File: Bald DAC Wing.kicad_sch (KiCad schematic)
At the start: 50 parts, among them J1 Power_In, J2 DAC_A_Out, J3 DAC_B_Out, U1 AD5447, U2 AD8065ARTZ, U3 AD8065ARTZ, U4 74LVC574APWR, U5 74LVC574APWR, U6 74LVC14, U7 REF3425

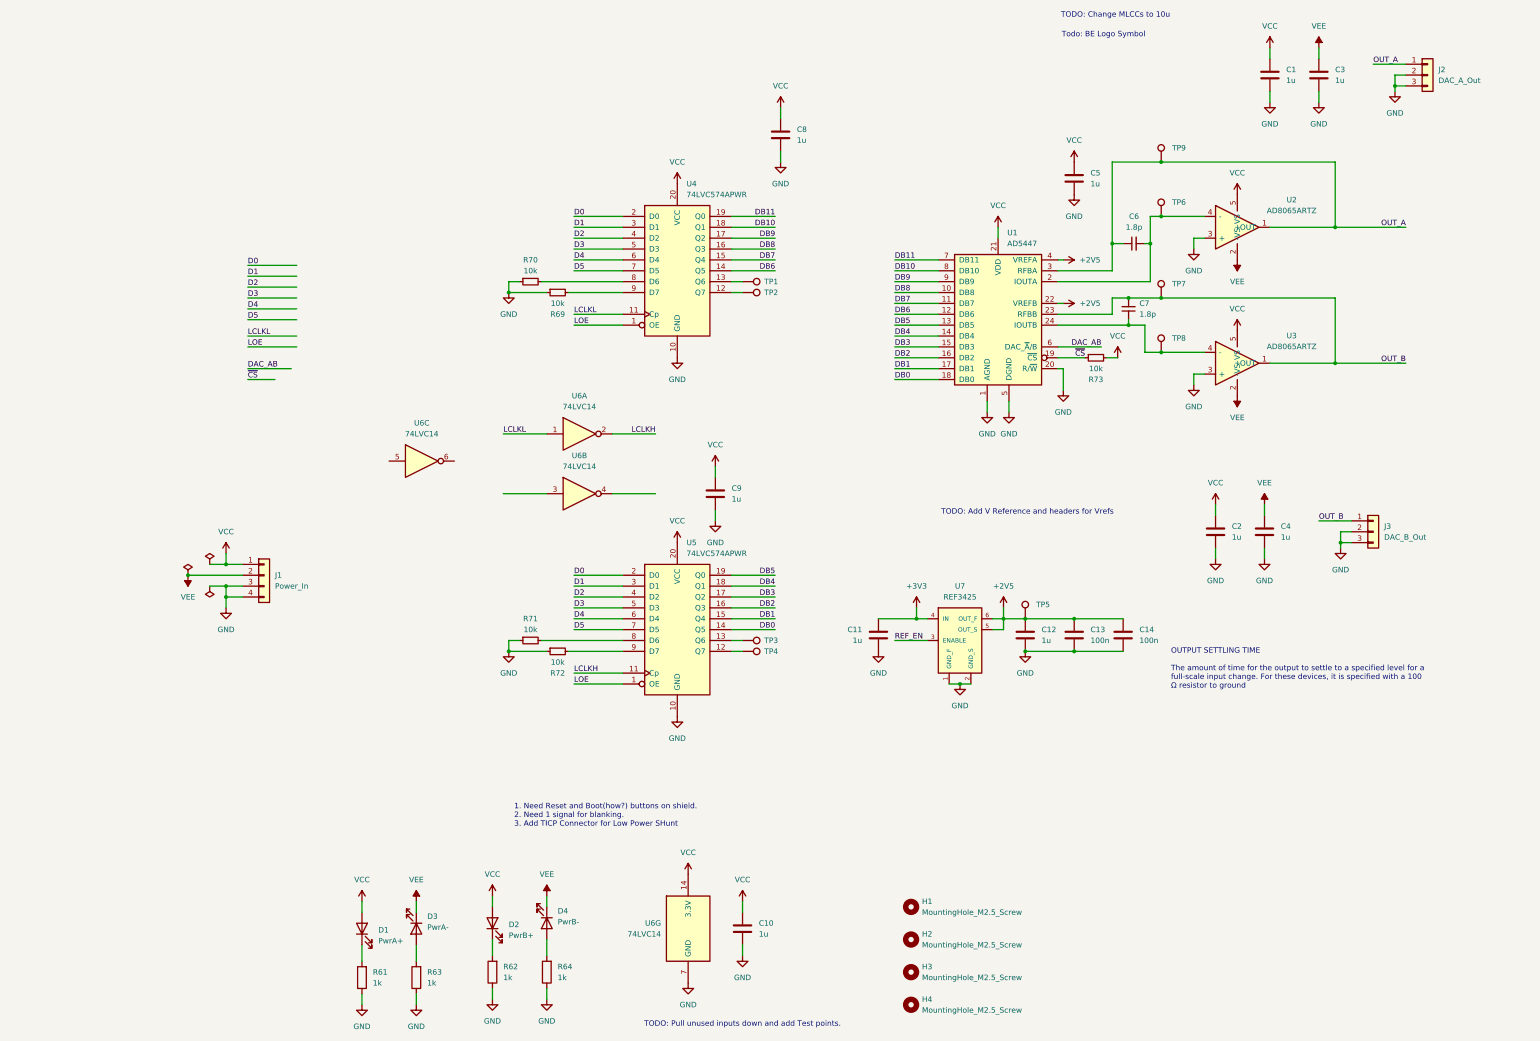
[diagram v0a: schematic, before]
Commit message: updated part numbs and changed to 1 gate inverter
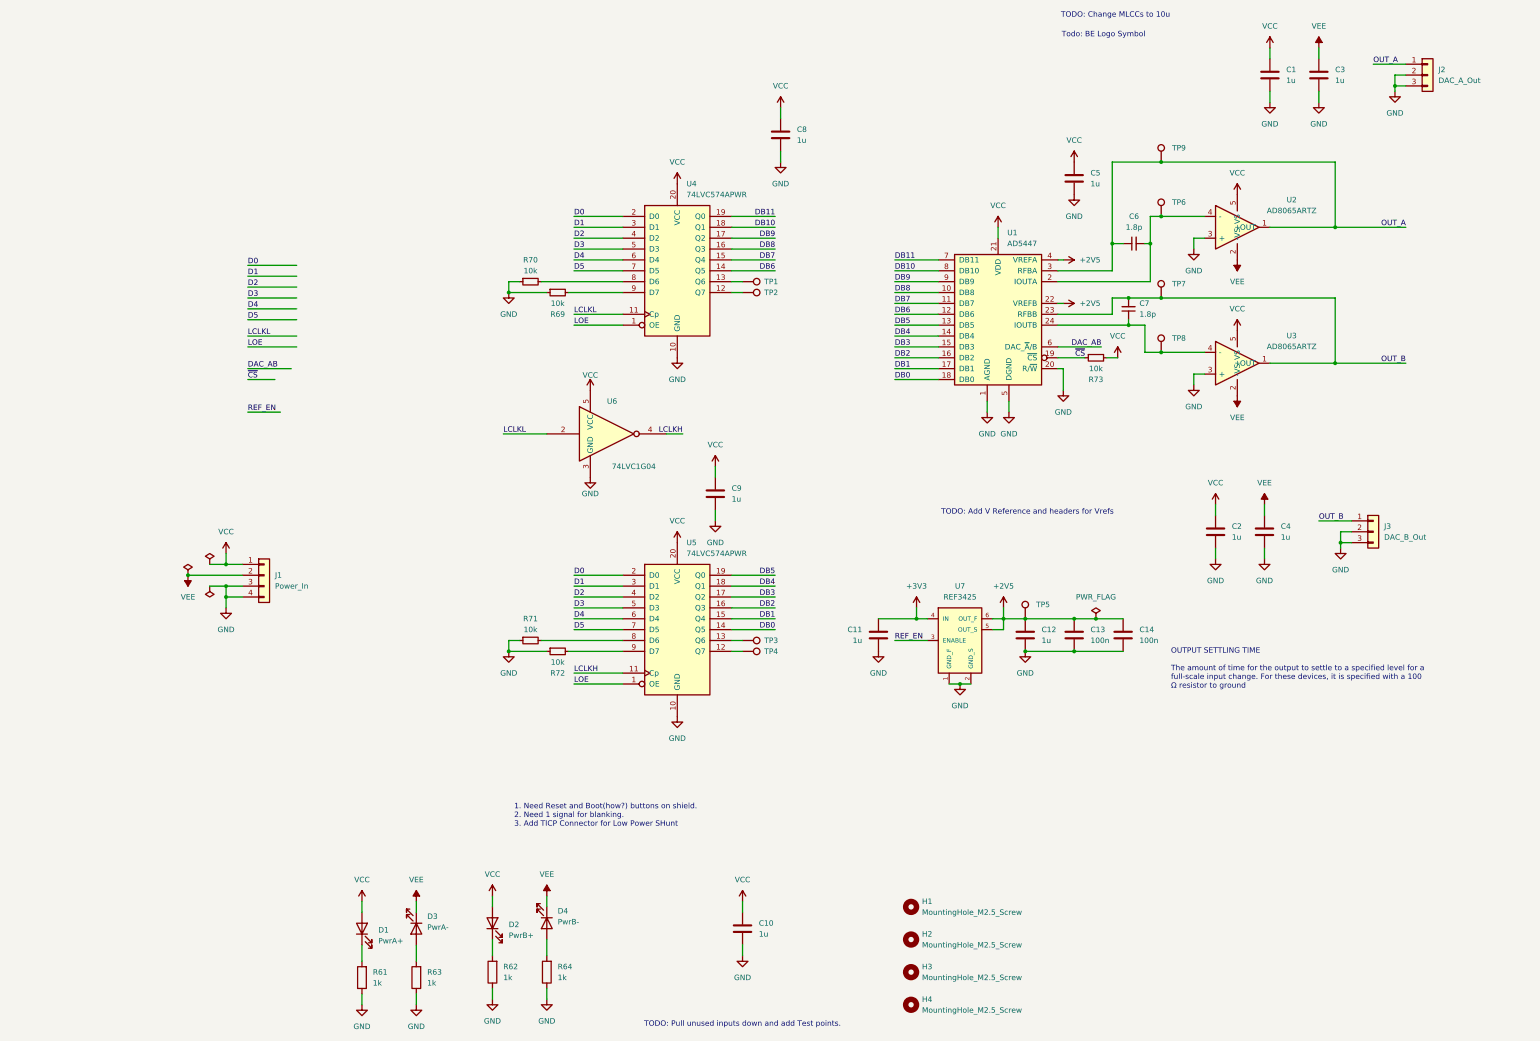
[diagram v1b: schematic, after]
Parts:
- removed U6: 74LVC14, Package_SO:TSSOP-14_4.4x5mm_P0.65mm, symbol 74xx:74LV14
- added U6: 74LVC1G04, Package_TO_SOT_SMD:SOT-23-5, symbol 74xGxx:74LVC1G04
- C13, C14: LCSC (none) -> C49678
- C6, C7: footprint (none) -> Capacitor_SMD:C_0603_1608Metric_Pad1.08x0.95mm_HandSolder; LCSC (none) -> C282244
- R61, R62, R63, R64: LCSC (none) -> C21190
- R69, R70, R71, R72, R73: LCSC (none) -> C25804
- TP1, TP2, TP3, TP4, TP5, TP6, TP7, TP8, TP9: LCSC (none) -> C3029083
- U1: LCSC (none) -> C514217
- U2, U3: LCSC (none) -> C9648
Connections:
- net GND: now also U6.3 (GND)
- net LCLKH: now also U6.4
- net LCLKL: now also U6.2
- net VCC: now also U6.5 (VCC)

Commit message: updated some caps
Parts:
- added C15: 1u, Capacitor_SMD:C_0805_2012Metric_Pad1.18x1.45mm_HandSolder, symbol Device:C
- C1, C10, C2, C3, C4, C5, C8, C9: value 1u -> 10uF; LCSC C28323 -> C380347
- H1, H2, H3, H4, J2, J3: now left out of the parts list
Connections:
- net GND: now also C15.2
- net VCC: now also C15.1

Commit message: thinking wings
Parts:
- removed C3, C4: 10uF, Capacitor_SMD:C_0805_2012Metric_Pad1.18x1.45mm_HandSolder, symbol Device:C
- removed D3: PwrA-, LED_SMD:LED_0805_2012Metric_Pad1.15x1.40mm_HandSolder, symbol Device:LED
- removed D4: PwrB-, LED_SMD:LED_0805_2012Metric_Pad1.15x1.40mm_HandSolder, symbol Device:LED
- removed R63, R64: 1k, Resistor_SMD:R_0603_1608Metric_Pad0.98x0.95mm_HandSolder, symbol Device:R
- added J4: Data Debug HDR, symbol Connector_Generic:Conn_02x12_Odd_Even
- added J5: Needed GPIO, Connector_PinHeader_2.54mm:PinHeader_2x12_P2.54mm_Vertical, symbol Connector_Generic:Conn_02x12_Odd_Even
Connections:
- net VCC is gone; now on net +3V3: C1.1, C10.1, C15.1, C2.1, C5.1, C8.1, C9.1, D1.2 (A), D2.2 (A), J1.1 (Pin_1), R73.2, U1.21 (VDD), U2.5 (+VS), U3.5 (+VS), U4.20 (VCC), U5.20 (VCC), U6.5 (VCC)
- net D0: now also J5.2 (Pin_2)
- net D1: now also J5.4 (Pin_4)
- net D2: now also J5.6 (Pin_6)
- net D3: now also J5.8 (Pin_8)
- net D4: now also J5.10 (Pin_10)
- net D5: now also J5.12 (Pin_12)
- net DAC_AB: now also J5.20 (Pin_20)
- net DB0: now also J4.24 (Pin_24)
- net DB1: now also J4.22 (Pin_22)
- net DB10: now also J4.4 (Pin_4)
- net DB11: now also J4.2 (Pin_2)
- net DB2: now also J4.20 (Pin_20)
- net DB3: now also J4.18 (Pin_18)
- net DB4: now also J4.16 (Pin_16)
- net DB5: now also J4.14 (Pin_14)
- net DB6: now also J4.12 (Pin_12)
- net DB7: now also J4.10 (Pin_10)
- net DB8: now also J4.8 (Pin_8)
- net DB9: now also J4.6 (Pin_6)
- net GND: now also U2.2 (-VS), U3.2 (-VS), J4.1 (Pin_1), J4.11 (Pin_11), J4.13 (Pin_13), J4.15 (Pin_15), J4.17 (Pin_17), J4.19 (Pin_19), J4.21 (Pin_21), J4.23 (Pin_23), J4.3 (Pin_3), J4.5 (Pin_5), J4.7 (Pin_7), J4.9 (Pin_9), J5.1 (Pin_1), J5.11 (Pin_11), J5.13 (Pin_13), J5.15 (Pin_15), J5.17 (Pin_17), J5.19 (Pin_19), J5.21 (Pin_21), J5.23 (Pin_23), J5.24 (Pin_24), J5.3 (Pin_3), J5.5 (Pin_5), J5.7 (Pin_7), J5.9 (Pin_9)
- net LCLKL: now also J5.14 (Pin_14)
- net LOE: now also J5.16 (Pin_16)
- net REF_EN: now also J5.18 (Pin_18)
- net ~{CS}: now also J5.22 (Pin_22)
- removed net VEE: J1.2 (Pin_2), U2.2 (-VS), U3.2 (-VS)
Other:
- note added: "11 GPIO"

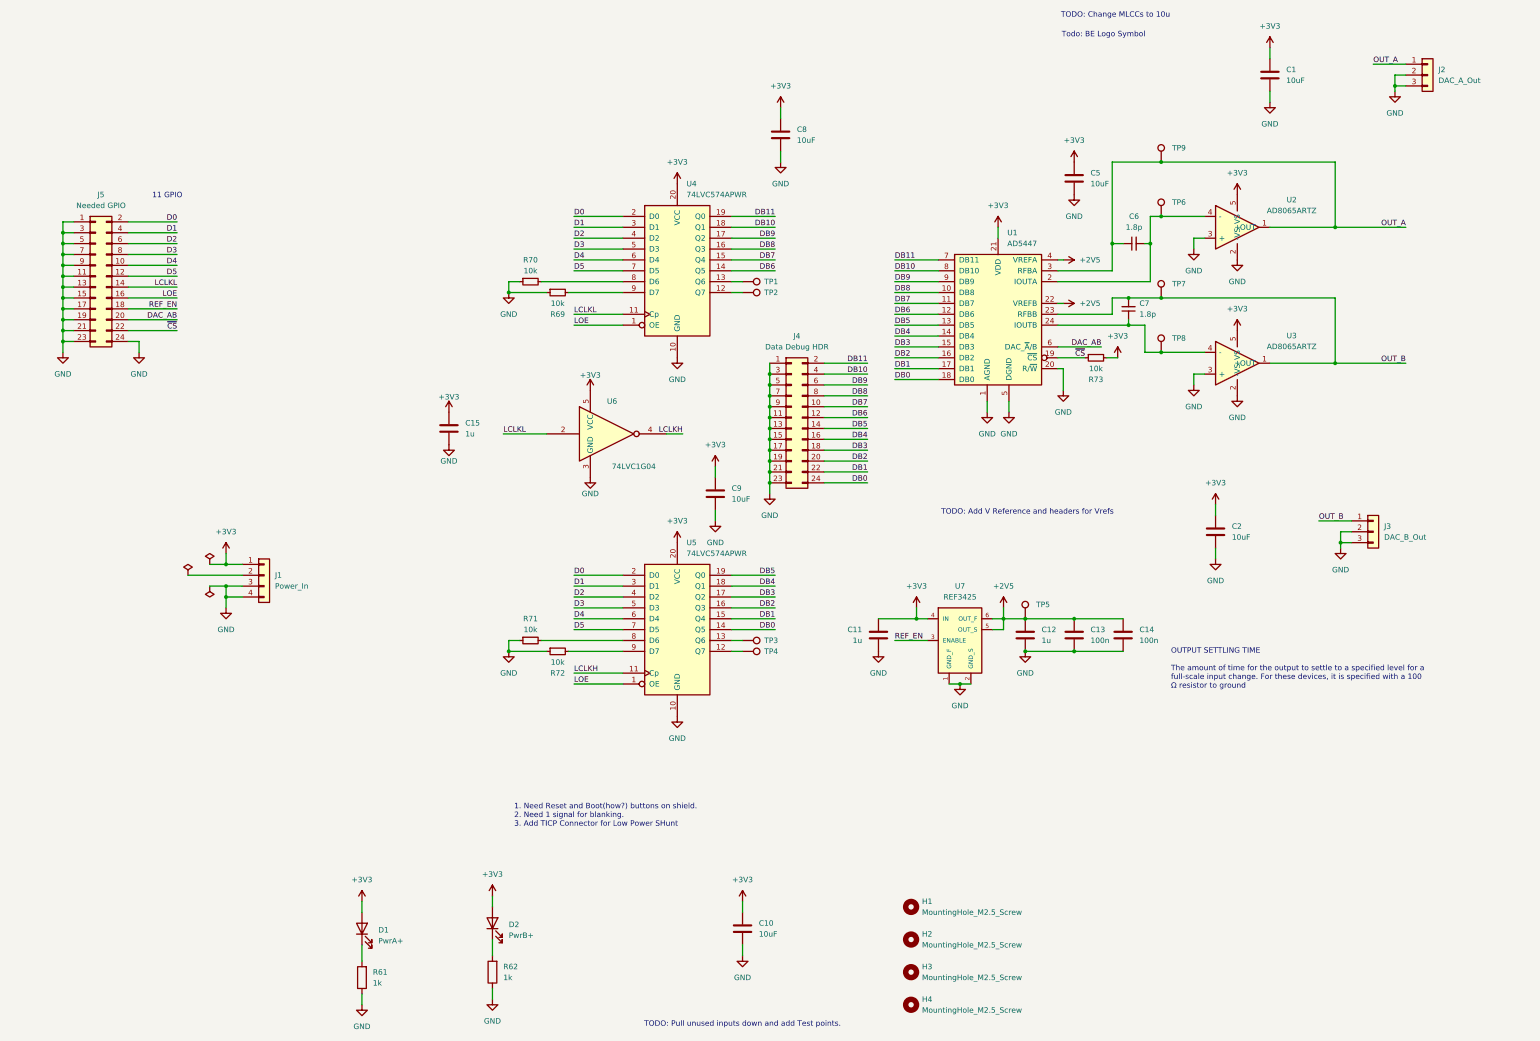
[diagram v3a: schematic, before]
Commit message: added adafruit wing and started wiring
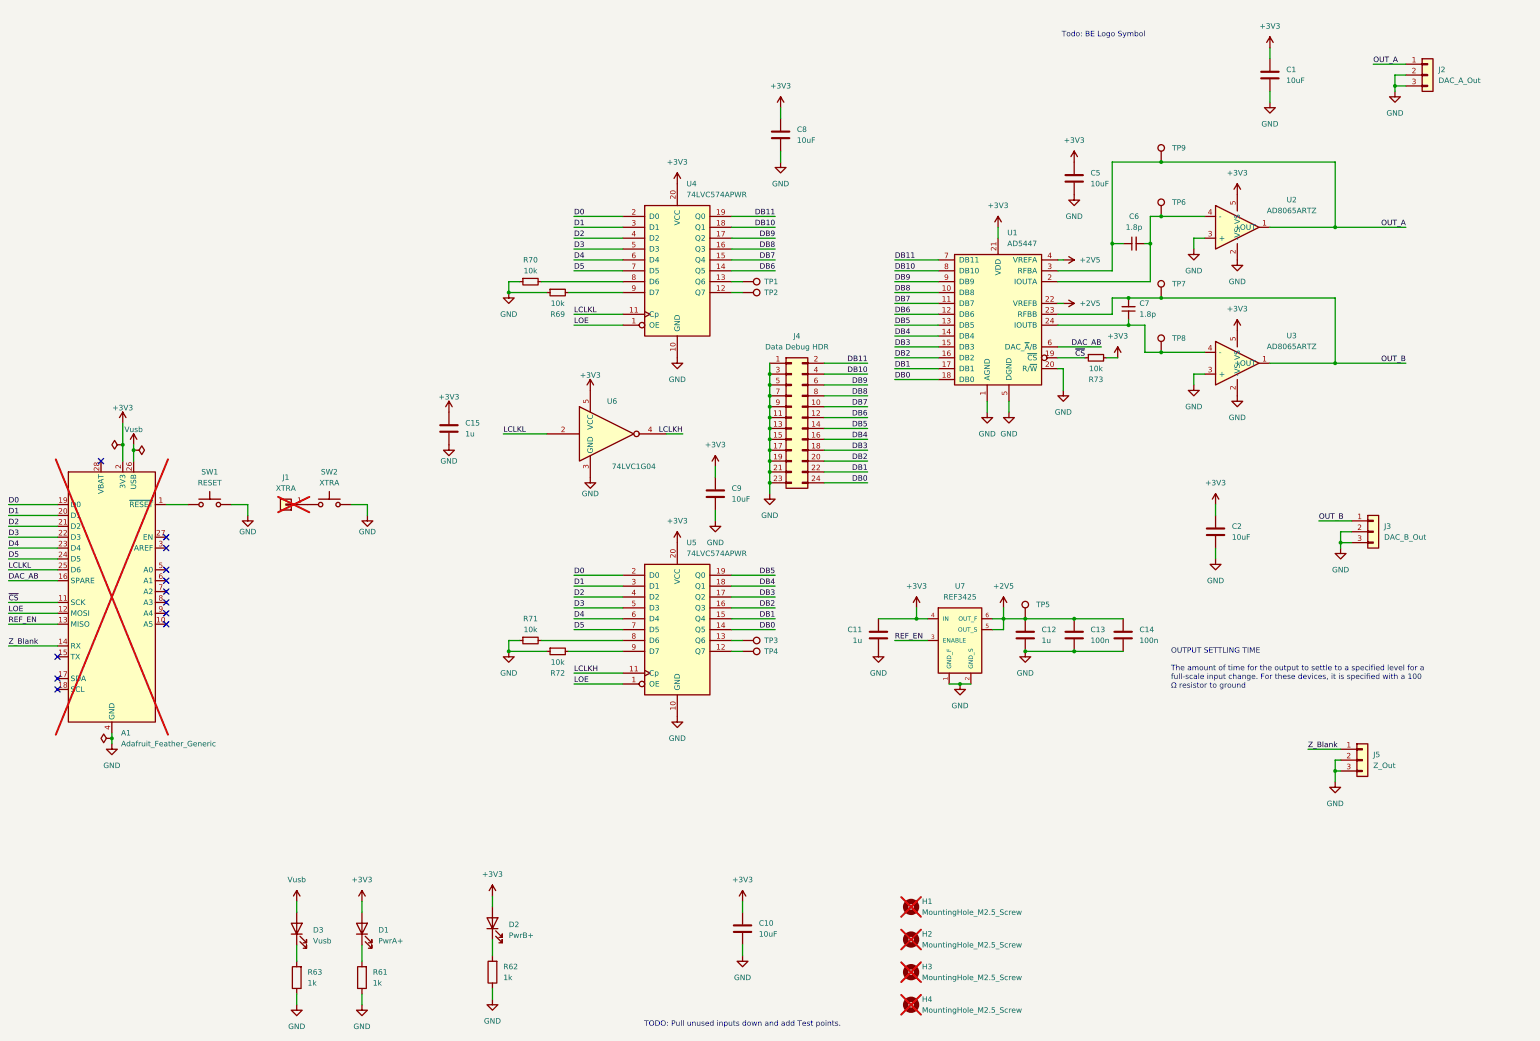
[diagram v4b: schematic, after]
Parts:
- removed J1: Power_In, LED_SMD:LED_0805_2012Metric_Pad1.15x1.40mm_HandSolder, symbol Connector_Generic:Conn_01x04
- removed J5: Needed GPIO, Connector_PinHeader_2.54mm:PinHeader_2x12_P2.54mm_Vertical, symbol Connector_Generic:Conn_02x12_Odd_Even
- added A1: Adafruit_Feather_Generic, Module:Adafruit_Feather, symbol MCU_Module:Adafruit_Feather_Generic
- added D3: Vusb, LED_SMD:LED_0805_2012Metric_Pad1.15x1.40mm_HandSolder, symbol Device:LED
- added J1: XTRA, Connector_PinSocket_2.54mm:PinSocket_1x01_P2.54mm_Vertical, symbol Connector_Generic:Conn_01x01
- added J5: Z_Out, Connector_PinHeader_2.54mm:PinHeader_1x03_P2.54mm_Vertical, symbol Connector_Generic:Conn_01x03
- added R63: 1k, Resistor_SMD:R_0603_1608Metric_Pad0.98x0.95mm_HandSolder, symbol Device:R
- added SW1: RESET, symbol Switch:SW_Push
- added SW2: XTRA, symbol Switch:SW_Push
- H1, H2, H3, H4: now not fitted
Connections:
- net +3V3: now also A1.2 (3V3)
- net D0: now also A1.19 (D0)
- net D1: now also A1.20 (D1)
- net D2: now also A1.21 (D2)
- net D3: now also A1.22 (D3)
- net D4: now also A1.23 (D4)
- net D5: now also A1.24 (D5)
- net DAC_AB: now also A1.16 (SPARE)
- net GND: now also A1.4 (GND), J5.2 (Pin_2), J5.3 (Pin_3), R63.1, SW1.2, SW2.2
- net LCLKL: now also A1.25 (D6)
- net LOE: now also A1.12 (MOSI)
- net REF_EN: now also A1.13 (MISO)
- net ~{CS}: now also A1.11 (SCK)
- new net: A1.1 (~{RESET}), SW1.1
- new net: D3.1 (K), R63.2
- new net: J1.1 (Pin_1), SW2.1
- new net Vusb: A1.26 (USB), D3.2 (A)
- new net Z_Blank: A1.14 (RX), J5.1 (Pin_1)
- no-connect marks 0 -> 12
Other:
- note removed: "1. Need Reset and Boot(how?) buttons on shield. 2. Need 1 signal for blanking. 3. Add TICP Connector for Low Power SHunt"
- note removed: "11 GPIO"
- note removed: "TODO: Add V Reference and headers for Vrefs"
- note removed: "TODO: Change MLCCs to 10u"

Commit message: minor changes before astra review
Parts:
- added TP10, TP11: TestPoint_Harwin, My Libraries:Harwin-S1751-46-Test-Point, symbol My Library:TestPoint_Harwin
- J4: symbol Connector_Generic:Conn_02x12_Odd_Even -> Connector_Generic:Conn_02x16_Odd_Even
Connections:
- net +3V3: now also TP11.1
- net DAC_AB: now also J4.26 (Pin_26)
- net GND: now also J4.25 (Pin_25), J4.27 (Pin_27), J4.29 (Pin_29)
- net LCLKH: now also J4.32 (Pin_32)
- net LCLKL: now also J4.30 (Pin_30)
- net LOE: now also TP10.1
- net ~{CS}: now also J4.28 (Pin_28)
